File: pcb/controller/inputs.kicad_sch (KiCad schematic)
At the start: 3 parts, among them SW1 SW_Push, SW2 SW_Push

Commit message: retraced target pcb
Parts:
- SW1, SW2: value SW_Push -> B3F-4055; footprint (none) -> external_footprints.petty:SW_B3F-4055
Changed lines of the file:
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@@
 			)
 		)
-		(property "Datasheet" ""
+		(property "Datasheet" "https://www.lcsc.com/datasheet/C143801.pdf"
 			(at 106.68 107.95 0)
 			(effects
@@
 	(symbol
 		(lib_id "Switch:SW_Push")
+		(at 91.44 78.74 0)
+		(unit 1)
+		(exclude_from_sim no)
+		(in_bom yes)
+		(on_board yes)
+		(dnp no)
+		(fields_autoplaced yes)
+		(property "Reference" "SW1"
+			(at 91.44 71.12 0)
+			(effects
+				(font
+					(size 1.27 1.27)
+				)
+			)
+		)
+		(property "Value" "B3F-4055"
+			(at 91.44 73.66 0)
+			(effects
+				(font
+					(size 1.27 1.27)
+				)
+			)
+		)
+		(property "Footprint" "external_footprints.petty:SW_B3F-4055"
+			(at 91.44 73.66 0)
+			(effects
+				(font
+					(size 1.27 1.27)
+				)
+				(hide yes)
+			)
+		)
+		(property "Datasheet" "~"
+			(at 91.44 73.66 0)
+			(effects
+				(font
+					(size 1.27 1.27)
+				)
+				(hide yes)
+			)
+		)
+		(property "Description" "Push button switch, generic, two pins"
+			(at 91.44 78.74 0)
+			(effects
+				(font
+					(size 1.27 1.27)
+				)
+				(hide yes)
+			)
+		)
+		(pin "1"
+		)
+		(pin "2"
+		)
+		(instances
+			(project "controller"
+				(path "/c599d8cf-7937-49be-b4ed-eac09167ead4/4b69996c-053f-4d78-af06-905aa0140461"
+					(reference "SW1")
+					(unit 1)
+				)
+			)
+		)
+	)
+	(symbol
+		(lib_id "Switch:SW_Push")
 		(at 91.44 90.17 0)
 		(unit 1)
@@
 			)
 		)
-		(property "Value" "SW_Push"
+		(property "Value" "B3F-4055"
 			(at 91.44 85.09 0)
 			(effects
@@
 			)
 		)
-		(property "Footprint" ""
+		(property "Footprint" "external_footprints.petty:SW_B3F-4055"
 			(at 91.44 85.09 0)
 			(effects
@@
 					(unit 1)
 				)
-			)
-		)
-	)
-	(symbol
-		(lib_id "Switch:SW_Push")
-		(at 91.44 78.74 0)
-		(unit 1)
-		(exclude_from_sim no)
-		(in_bom yes)
-		(on_board yes)
-		(dnp no)
-		(fields_autoplaced yes)
-		(property "Reference" "SW1"
-			(at 91.44 71.12 0)
-			(effects
-				(font
-					(size 1.27 1.27)
-				)
-			)
-		)
-		(property "Value" "SW_Push"
-			(at 91.44 73.66 0)
-			(effects
-				(font
-					(size 1.27 1.27)
-				)
-			)
-		)
-		(property "Footprint" ""
-			(at 91.44 73.66 0)
-			(effects
-				(font
-					(size 1.27 1.27)
-				)
-				(hide yes)
-			)
-		)
-		(property "Datasheet" "~"
-			(at 91.44 73.66 0)
-			(effects
-				(font
-					(size 1.27 1.27)
-				)
-				(hide yes)
-			)
-		)
-		(property "Description" "Push button switch, generic, two pins"
-			(at 91.44 78.74 0)
-			(effects
-				(font
-					(size 1.27 1.27)
-				)
-				(hide yes)
-			)
-		)
-		(pin "1"
-		)
-		(pin "2"
-		)
-		(instances
-			(project ""
-				(path "/c599d8cf-7937-49be-b4ed-eac09167ead4/4b69996c-053f-4d78-af06-905aa0140461"
-					(reference "SW1")
-					(unit 1)
-				)

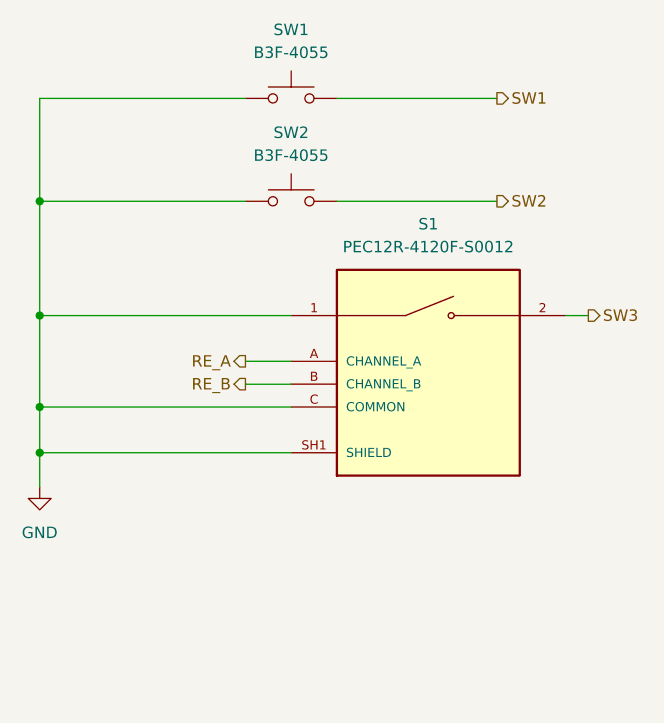
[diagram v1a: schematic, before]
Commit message: added lcsc numbers to all components and added ESD protection
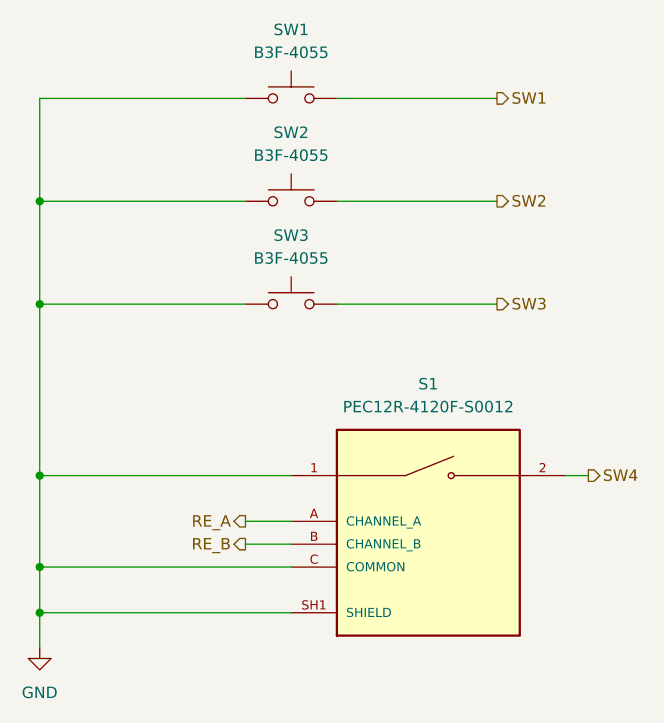
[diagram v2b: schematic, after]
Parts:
- added SW3: B3F-4055, external_footprints.petty:SW_B3F-4055, symbol Switch:SW_Push
- S1: footprint PEC12R-4120F-S0012:XDCR_PEC12R-4120F-S0012 -> external_footprints.petty:XDCR_PEC12R-4120F-S0012; LCSC (none) -> C143801
- SW1, SW2: LCSC (none) -> C36498965
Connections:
- net GND: now also SW3.1
- net SW3: now also SW3.2; no longer S1.2
- new net SW4: S1.2
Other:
- moved on the sheet: S1
